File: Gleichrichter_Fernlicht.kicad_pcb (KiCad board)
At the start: 2 copper layers, 27.9 x 28 mm, 16 parts, among them Q1 Q_NMOS_GDS, Q2 Q_PMOS_GDS, Q3 Q_PMOS_GDS, Q4 Q_NMOS_GDS

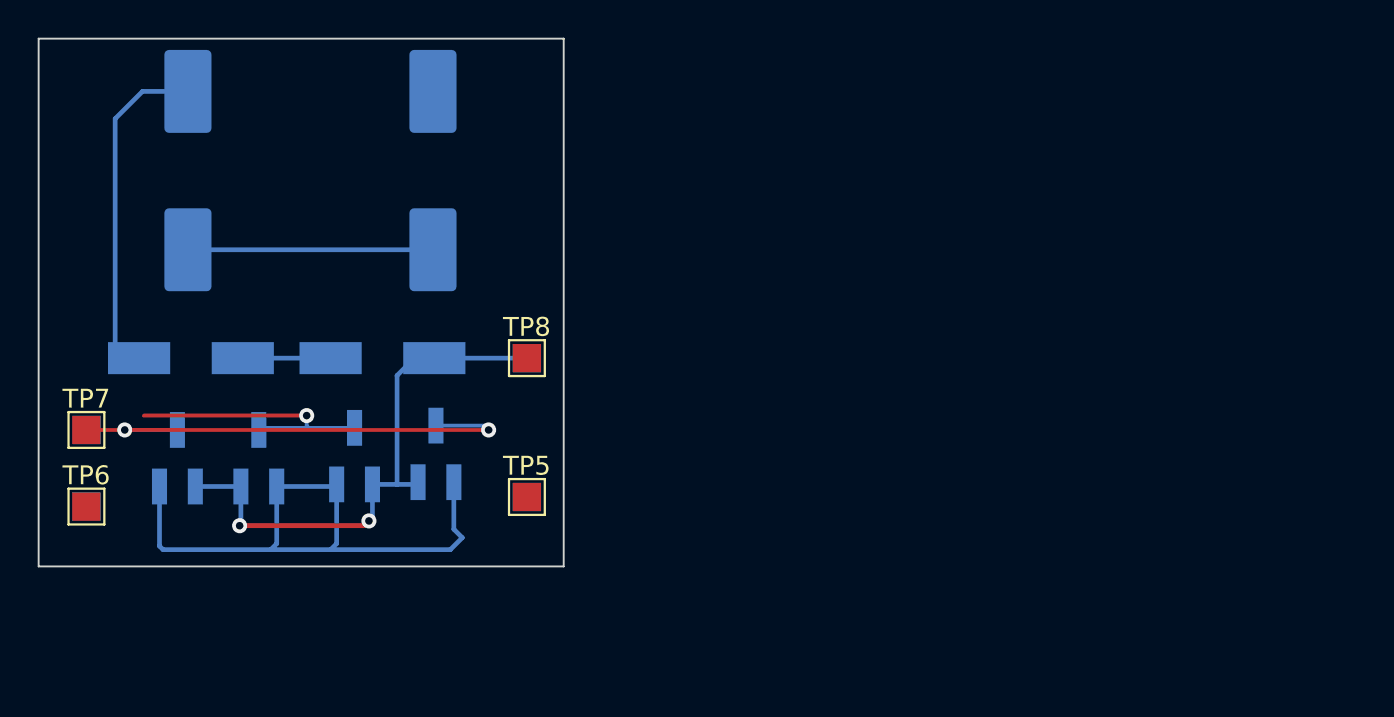
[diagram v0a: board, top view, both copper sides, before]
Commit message: Kontur von Jan importiert und gelayoutet. Evtl. noch Kupferflaechen machen?
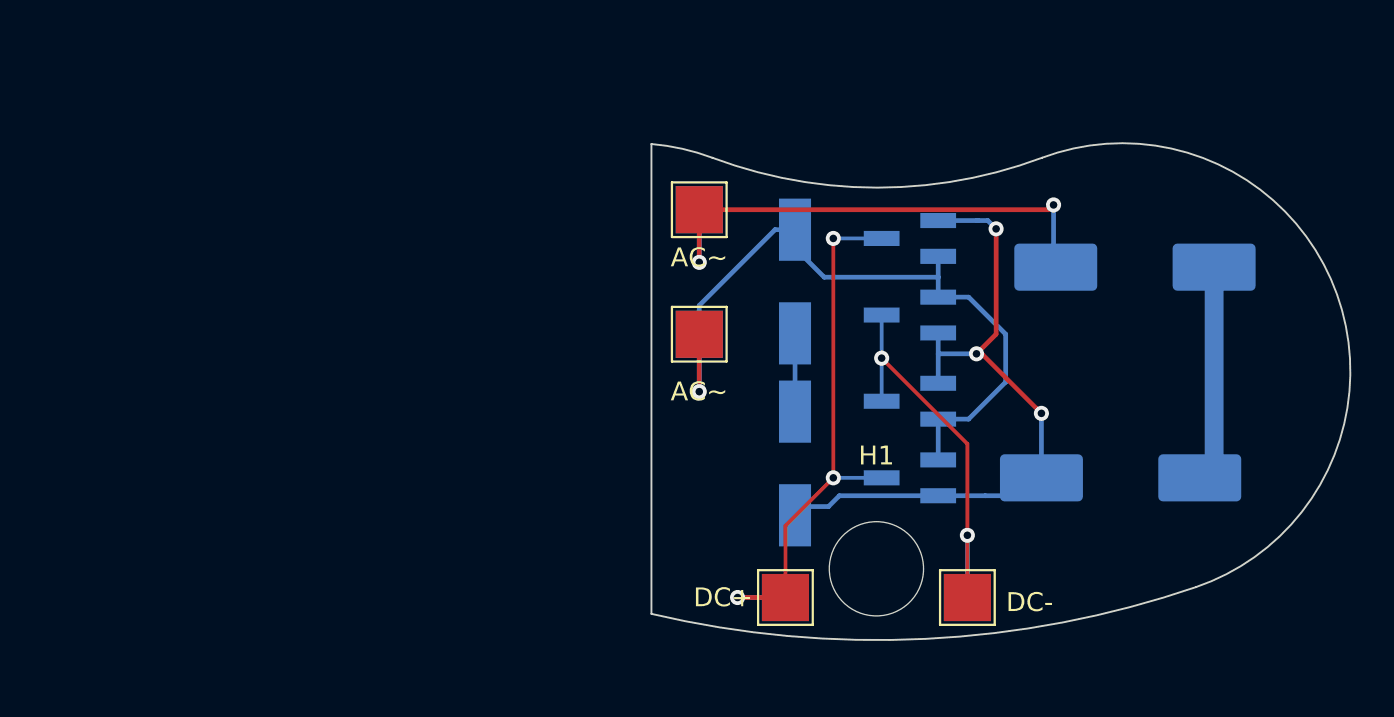
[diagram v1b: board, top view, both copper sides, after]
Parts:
- added H1: MountingHole, MountingHole:MountingHole_5mm, F.Cu at (144.5, 119.1)
- TP1, TP2, TP3, TP4, TP5, TP6, TP7, TP8: footprint TestPoint:TestPoint_Pad_1.5x1.5mm -> TestPoint:TestPoint_Pad_2.5x2.5mm
- moved C2 52.1 mm to (157.5, 114.3), turned to 180 degrees
- moved TP2 47.0 mm to (149.4, 120.7), turned to -90 degrees
- moved TP6 47.0 mm to (149.4, 120.7), turned to 90 degrees
- moved Q2 38.9 mm to (146.3, 114.3), turned to 180 degrees
- moved TP3 38.1 mm to (139.7, 120.7), turned to -90 degrees
- moved TP7 38.1 mm to (139.7, 120.7), turned to 90 degrees
- moved C1 37.6 mm to (158.2, 103.1), turned to 180 degrees
- moved Q3 34.7 mm to (146.3, 110.2), turned to 180 degrees
- moved D1 32.5 mm to (140.2, 113.5), turned to 90 degrees
- moved Q1 30.4 mm to (146.3, 105.7), turned to 180 degrees
- moved Q4 27.6 mm to (146.3, 101.6), turned to 180 degrees
- moved D2 22.3 mm to (140.2, 103.9), turned to -90 degrees
- moved TP1 17.8 mm to (135.1, 100.1), turned to -90 degrees
- moved TP5 17.8 mm to (135.1, 100.1), turned to 90 degrees
- moved TP4 9.23 mm to (135.1, 106.7)
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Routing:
- net DYN_1: track 0.28 -> 27.8 mm, vias 0 -> 2
- net Net-(C2-Pad2): track 50.2 -> 37.2 mm, vias 0 -> 3
- net DYN_2: track 29.0 -> 39.2 mm, vias 2 -> 1
- net DC-: track 14.5 -> 22.5 mm, vias 1 -> 2
- net DC+: track 27.0 -> 30.3 mm, vias 2 -> 3
- net Net-(C1-Pad1): track 13.0 -> 11.5 mm
- net Net-(D1-Pad2): track 4.66 -> 4.15 mm
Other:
- board size 27.9 x 28 mm -> 37.1 x 26.4 mm
- board text added: "AC~"
- board text added: "DC+"
- board text added: "DC-"

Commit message: Stand der zu jlcpcb geschickt wurde
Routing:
- net DYN_2: track 39.2 -> 38.6 mm
- added copper zone on B.Cu, net DC-
- added copper zone on F.Cu, net DC-
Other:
- board text added: "Fernlicht_PCB_V1"

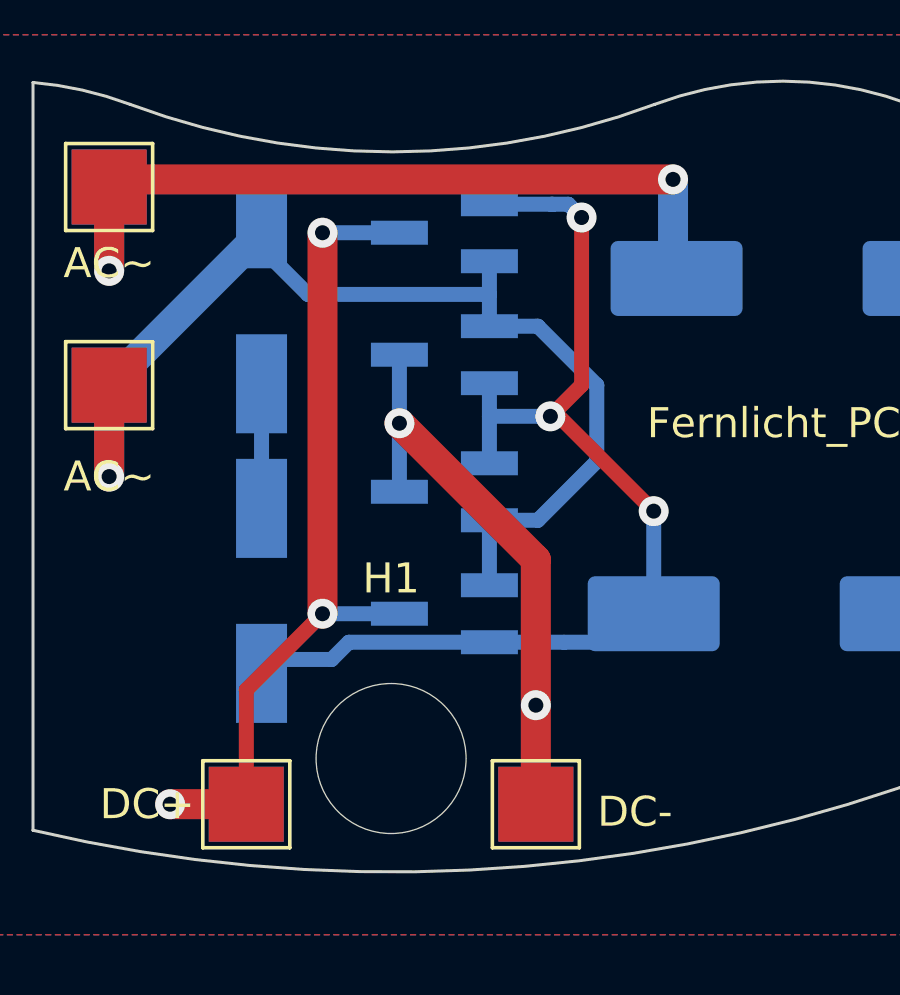
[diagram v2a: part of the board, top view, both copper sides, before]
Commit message: Standard Mosfet-Symbol hat nicht zu SOT-23 Footprint gepasst. (Drain und Source vertauscht). Jetzt korrigiert. Layout noch nicht fertig. Hotfix: Transistoren auf erster Platine verkehrt herum drauflöten
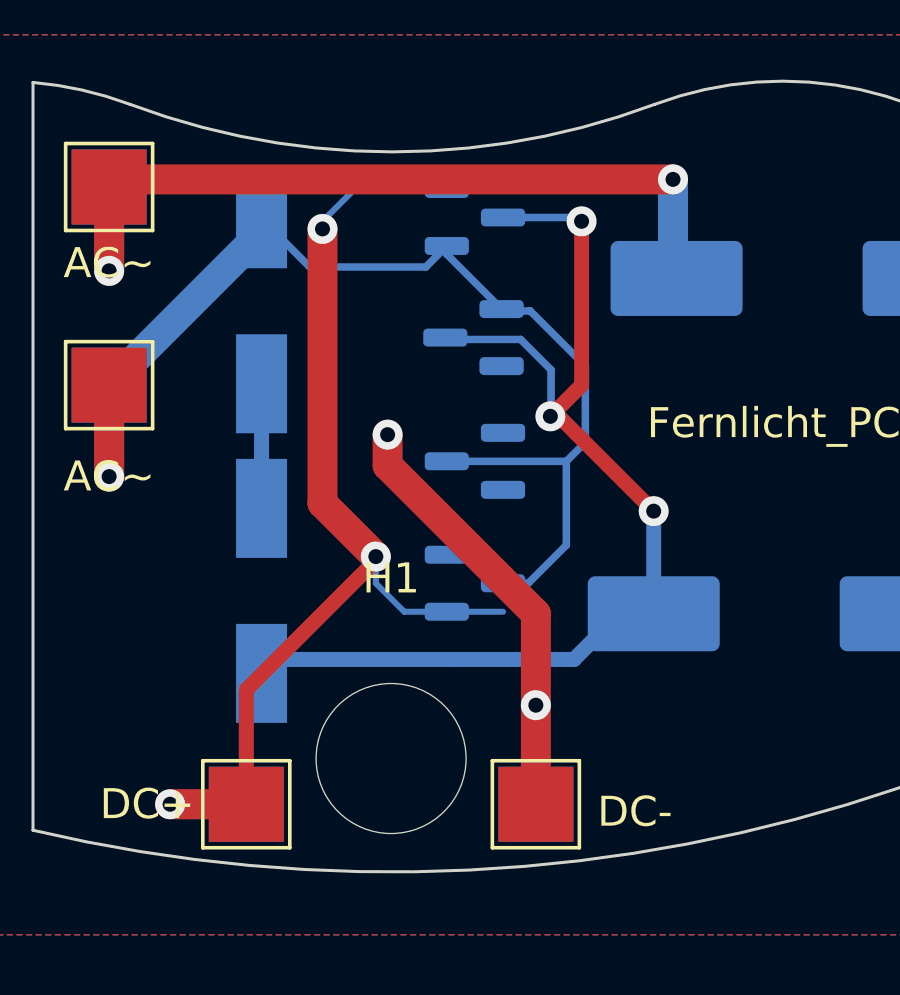
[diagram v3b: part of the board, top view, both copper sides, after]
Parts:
- Q1: value Q_NMOS_GDS -> 2N7002; footprint Package_TO_SOT_SMD:SOT-23_Handsoldering -> Package_TO_SOT_SMD:SOT-23
- Q2: value Q_PMOS_GDS -> AO3401A; footprint Package_TO_SOT_SMD:SOT-23_Handsoldering -> Package_TO_SOT_SMD:SOT-23
- Q3: value Q_PMOS_GDS -> 2N7002; footprint Package_TO_SOT_SMD:SOT-23_Handsoldering -> Package_TO_SOT_SMD:SOT-23
- Q4: value Q_NMOS_GDS -> AO3401A; footprint Package_TO_SOT_SMD:SOT-23_Handsoldering -> Package_TO_SOT_SMD:SOT-23
- moved Q2 13.2 mm to (147.3, 101.1), turned to 0 degrees
- moved Q4 11.7 mm to (147.3, 113.3), turned to 0 degrees
- moved Q3 1.44 mm to (147.3, 109.2)
- moved Q1 1.12 mm to (147.3, 105.1)
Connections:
- Q1 pad 2: Net-(C2-Pad2) -> DC-
- Q1 pad 3: DC- -> Net-(C2-Pad2)
- Q2 pad 2: Net-(C2-Pad2) -> DC+
- Q2 pad 3: DC+ -> Net-(C2-Pad2)
- Q3 pad 2: DYN_2 -> DC-
- Q3 pad 3: DC- -> DYN_2
- Q4 pad 2: DYN_2 -> DC+
- Q4 pad 3: DC+ -> DYN_2
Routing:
- net DC+: track 30.3 -> 37.2 mm
- net DC-: track 22.5 -> 17.8 mm
- net DYN_2: track 38.6 -> 42.1 mm

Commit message: update: Layout korrigiert und an jlc geschickt
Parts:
- added D3: ZD_16, Diode_SMD:D_MiniMELF_Handsoldering, B.Cu at (134.6, 115.8)
- added D4: ZD_16, Diode_SMD:D_MiniMELF_Handsoldering, B.Cu at (140.2, 105.4)
- D1, D2: footprint Diode_SMD:D_MiniMELF_Handsoldering -> Diode_SMD:D_SOD-123
- Q1, Q2, Q3, Q4: footprint Package_TO_SOT_SMD:SOT-23 -> Package_TO_SOT_SMD:SOT-23_Handsoldering
- moved D1 6.02 mm to (143.0, 108.2)
- moved D2 2.90 mm to (143.0, 103.1)
- moved Q4 1.52 mm to (147.3, 111.8), turned to 180 degrees
- moved Q3 1.02 mm to (147.3, 108.2)
- moved Q1 0.45 mm to (147.3, 104.6), turned to 0 degrees
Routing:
- net Net-(D1-K): track 37.2 -> 59.4 mm, vias 3 -> 0
- net Net-(D1-A): track 4.15 -> 16.5 mm
- net DC-: track 17.8 -> 26.3 mm, vias 2 -> 3
- net DYN_2: track 42.1 -> 34.7 mm
- net DC+: track 37.2 -> 38.0 mm, vias 3 -> 4
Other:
- board text added: "Fernlicht_PCB_V1:1"
- board text removed: "Fernlicht_PCB_V1"
